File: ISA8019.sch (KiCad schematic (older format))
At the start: 22 parts

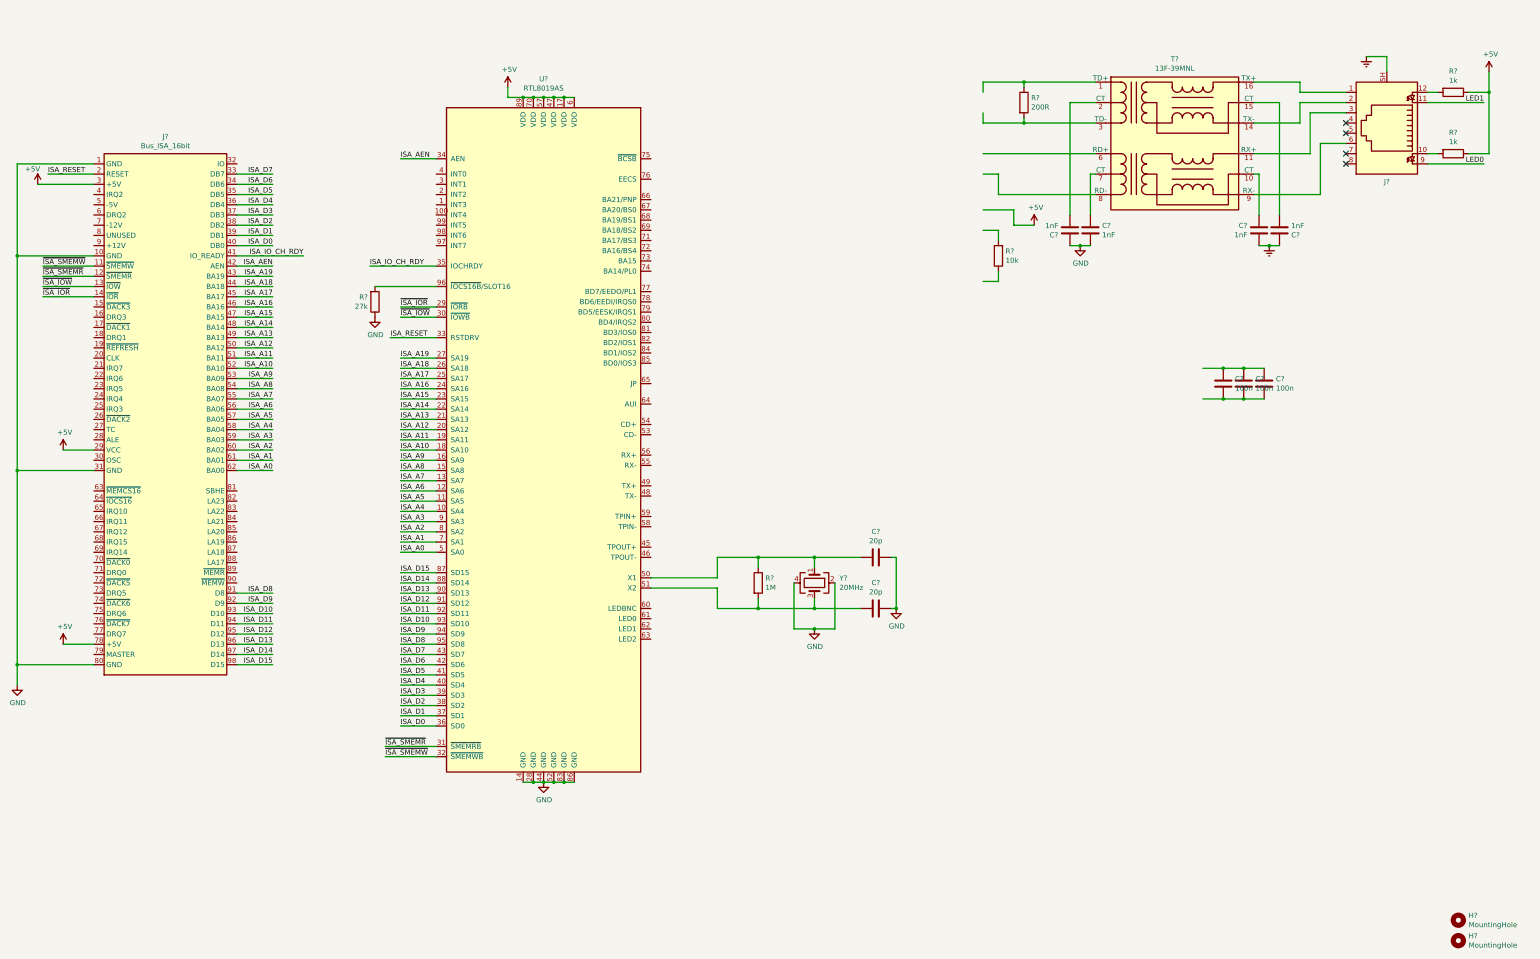
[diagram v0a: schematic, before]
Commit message: Add EEPROM and boot flash
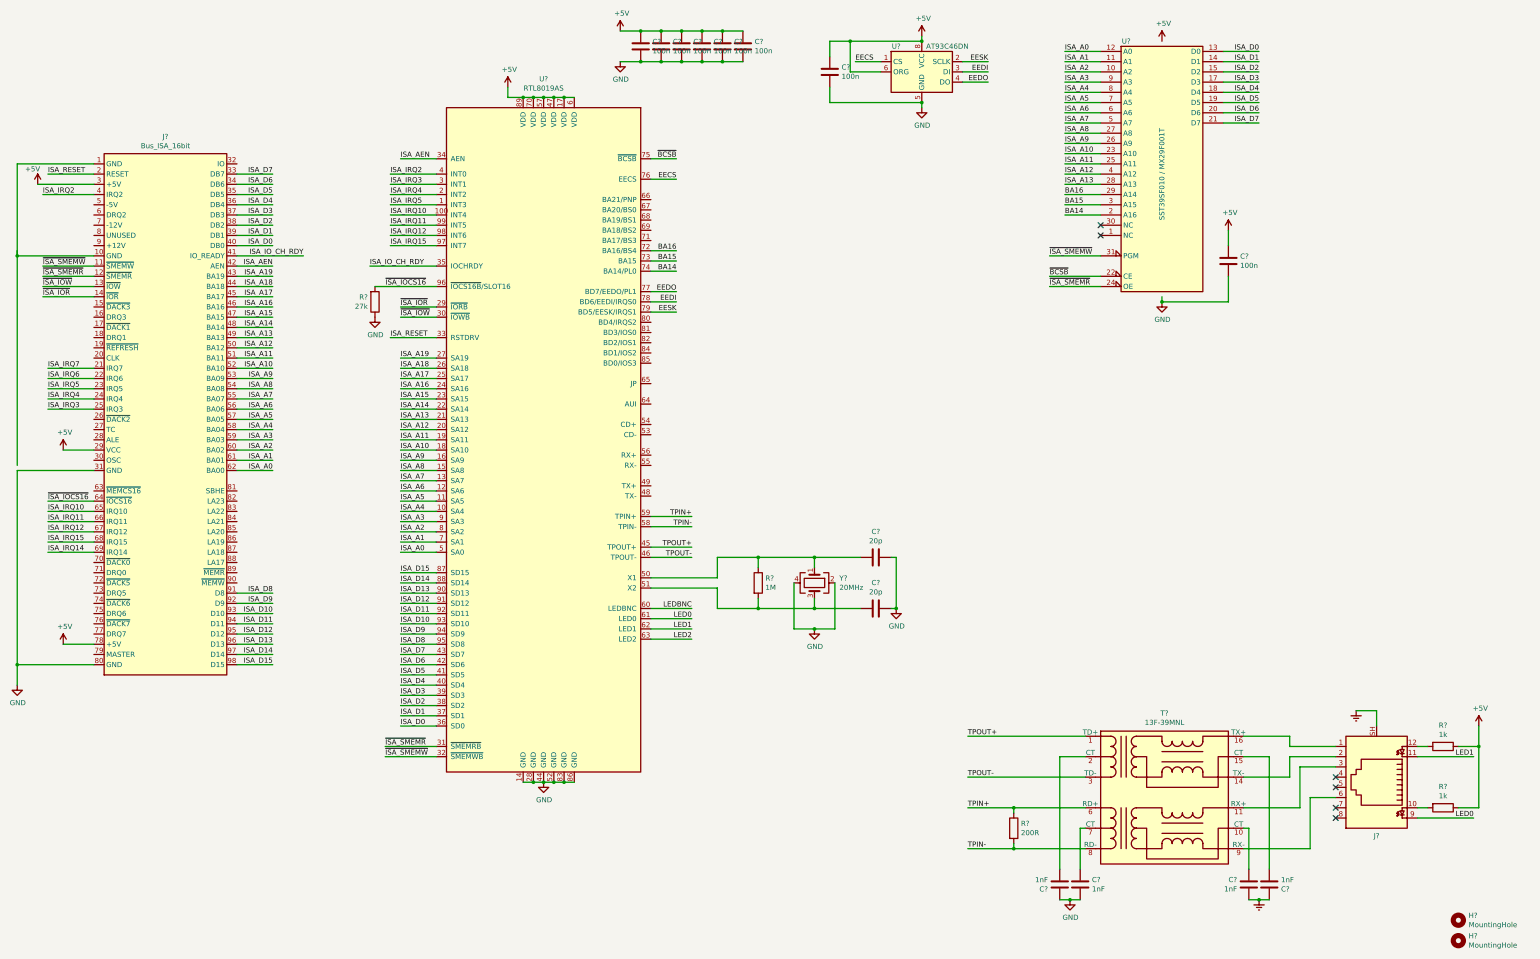
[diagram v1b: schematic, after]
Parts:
- removed R?: 10k, Resistor_SMD:R_0402_1005Metric, symbol Device:R
- added C? (x5): 100n, Capacitor_SMD:C_0402_1005Metric, symbol Device:C
- added U?: AT93C46DN, Package_SO:SOIC-8_3.9x4.9mm_P1.27mm, symbol Memory_EEPROM:93CxxC
- added U?: SST39SF010 / MX29F001T, Package_DIP:DIP-32_W15.24mm_Socket_LongPads, symbol Memory_Flash:SST39SF010
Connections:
- net labels added: BA14, BA15, BA16, EECS, EEDI, EEDO, EESK, ISA_IRQ10, ISA_IRQ11, ISA_IRQ12, ISA_IRQ14, ISA_IRQ15, ISA_IRQ2, ISA_IRQ3, ISA_IRQ4, ISA_IRQ5, ISA_IRQ6, ISA_IRQ7, LED2, LEDBNC, TPIN+, TPIN-, TPOUT+, TPOUT-, ~BCSB, ~ISA_IOCS16
- wire segments 190 -> 267
- no-connect marks 4 -> 6
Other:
- moved on the sheet: C?, J?, R?, T?

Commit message: Add jumpers, AUI interface
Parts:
- removed C? (x5): 100n, Capacitor_SMD:C_0402_1005Metric, symbol Device:C
- added C15, C3, C4, C5, C6: 100n, Capacitor_SMD:C_0402_1005Metric, symbol Device:C
- added C2: 47µF 10V, Capacitor_SMD:C_1206_3216Metric, symbol Device:C
- added J3: AUI, Connector_PinHeader_2.54mm:PinHeader_2x08_P2.54mm_Vertical, symbol Connector_Generic:Conn_02x08_Top_Bottom
- added J4: Jumper mode, Connector_PinHeader_2.54mm:PinHeader_2x01_P2.54mm_Vertical, symbol Connector_Generic:Conn_02x01
- added J5: PNP force, Connector_PinHeader_2.54mm:PinHeader_2x01_P2.54mm_Vertical, symbol Connector_Generic:Conn_02x01
- added J6: BROM size and base address, Connector_PinHeader_2.54mm:PinHeader_2x05_P2.54mm_Vertical, symbol Connector_Generic:Conn_02x05_Counter_Clockwise
- added J7: I/O base address, Connector_PinHeader_2.54mm:PinHeader_2x04_P2.54mm_Vertical, symbol Connector_Generic:Conn_02x04_Counter_Clockwise
- added J8: Medium type, Connector_PinHeader_2.54mm:PinHeader_2x02_P2.54mm_Vertical, symbol Connector_Generic:Conn_02x02_Counter_Clockwise
- added J9: IRQ select, Connector_PinHeader_2.54mm:PinHeader_2x03_P2.54mm_Vertical, symbol Connector_Generic:Conn_02x03_Counter_Clockwise
- added R10, R11, R12, R13, R14, R15, R16, R17, R18, R19, R20, R21, R22, R6, R7, R8, R9: 10k, Resistor_SMD:R_0402_1005Metric, symbol Device:R
- J1: renamed from J?; footprint (none) -> Connector_PCBEdge:BUS_AT
- gave numbers to parts that had none: 22
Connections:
- net +5V: now also C15.1, C2.1, C3.1, C4.1, C5.1, C6.1, J4.2 (Pin_2), J5.2 (Pin_2), J6.10 (Pin_10), J6.6 (Pin_6), J6.7 (Pin_7), J6.8 (Pin_8), J6.9 (Pin_9), J7.5 (Pin_5), J7.6 (Pin_6), J7.7 (Pin_7), J7.8 (Pin_8), J8.3 (Pin_3), J8.4 (Pin_4), J9.4 (Pin_4), J9.5 (Pin_5), J9.6 (Pin_6)
- net BA14: now also R18.1
- net BA16: now also R13.1
- net GND: now also J1.1 (GND), J1.10 (GND), C15.2, C2.2, C3.2, C4.2, C5.2, C6.2, J3.1 (Pin_1), J3.11 (Pin_11), J3.14 (Pin_14), J3.4 (Pin_4), J3.6 (Pin_6), J3.8 (Pin_8), R6.2
- net ISA_D0: no longer U3.13 (D0)
- net ISA_D1: no longer U3.14 (D1)
- net ISA_D2: no longer U3.15 (D2)
- net ISA_D3: no longer U3.17 (D3)
- net ISA_D4: no longer U3.18 (D4)
- net ISA_D5: no longer U3.19 (D5)
- net ISA_D6: no longer U3.20 (D6)
- net ISA_D7: no longer U3.21 (D7)
- net +12V: now reaches J1.9 (+12V)
- net +12V: now also J3.13 (Pin_13)
- net TX-: now reaches U1.48 (TX-)
- net TX-: now also J3.10 (Pin_10)
- net TX+: now reaches U1.49 (TX+)
- net TX+: now also J3.3 (Pin_3)
- net CD-: now reaches U1.53 (CD-)
- net CD-: now also J3.9 (Pin_9)
- net CD+: now reaches U1.54 (CD+)
- net CD+: now also J3.2 (Pin_2)
- net RX-: now reaches U1.55 (RX-)
- net RX-: now also J3.12 (Pin_12)
- net RX+: now reaches U1.56 (RX+)
- net RX+: now also J3.5 (Pin_5)
- net AUI: now reaches U1.64 (AUI)
- net AUI: now also J3.16 (Pin_16), R6.1
- net JP: now reaches U1.65 (JP)
- net JP: now also R7.1
- net PNP: now reaches U1.66 (BA21/PNP)
- net PNP: now also R8.1
- net BS0: now reaches U1.67 (BA20/BS0)
- net BS0: now also R9.1
- net BS1: now reaches U1.68 (BA19/BS1)
- net BS1: now also R10.1
- net BS2: now reaches U1.69 (BA18/BS2)
- net BS2: now also R11.1
- net BS3: now reaches U1.71 (BA17/BS3)
- net BS3: now also R12.1
- net BD4: now reaches U1.80 (BD4/IRQS2)
- net BD4: now also U3.18 (D4), R22.1
- net BD3: now reaches U1.81 (BD3/IOS0)
- net BD3: now also U3.17 (D3), R14.1
- net BD2: now reaches U1.82 (BD2/IOS1)
- net BD2: now also U3.15 (D2), R15.1
- net BD1: now reaches U1.84 (BD1/IOS2)
- net BD1: now also U3.14 (D1), R16.1
- net BD0: now reaches U1.85 (BD0/IOS3)
- net BD0: now also U3.13 (D0), R17.1
- net EEDI renamed BD6
- net BD6: now also U3.20 (D6), R20.1
- net EEDO renamed BD7
- net BD7: now also U3.21 (D7), R19.1
- net EESK renamed BD5
- net BD5: now also U3.19 (D5), R21.1
- new net: J6.1 (Pin_1), R9.2
- new net: J6.2 (Pin_2), R10.2
- new net: J6.3 (Pin_3), R11.2
- new net: J6.4 (Pin_4), R12.2
- new net: J6.5 (Pin_5), R13.2
- new net: J4.1 (Pin_1), R7.2
- new net: J7.1 (Pin_1), R14.2
- new net: J7.2 (Pin_2), R15.2
- new net: J7.3 (Pin_3), R16.2
- new net: J7.4 (Pin_4), R17.2
- new net: J8.1 (Pin_1), R18.2
- new net: J8.2 (Pin_2), R19.2
- new net: J9.1 (Pin_1), R20.2
- new net: J9.2 (Pin_2), R21.2
- new net: J9.3 (Pin_3), R22.2
- new net: J5.1 (Pin_1), R8.2
- no-connect marks 6 -> 8
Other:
- note added: "Base-T Interface"
- note added: "Boot ROM"
- note added: "EEPROM"
- note added: "ISA-Bus"
- note added: "Jumpers"
- note added: "RTL8019"
- moved on the sheet: C1, C12, C7, J1, U2, U3

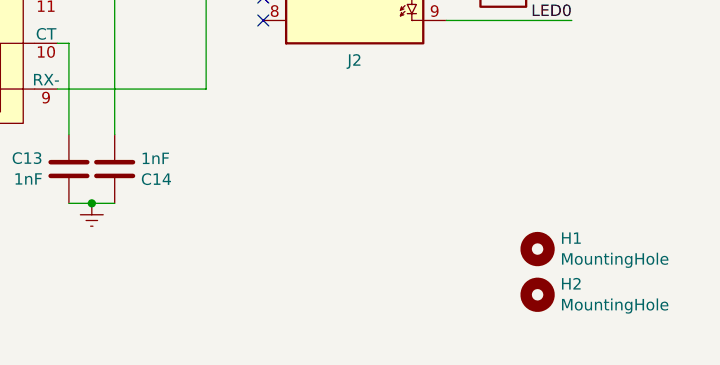
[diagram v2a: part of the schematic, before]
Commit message: Add mechanicals
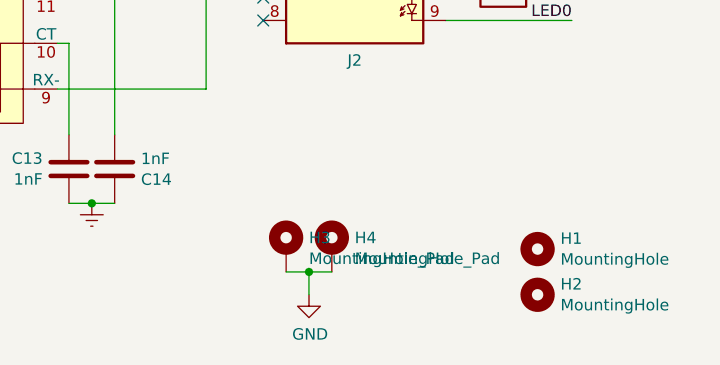
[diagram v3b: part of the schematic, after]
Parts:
- added H3, H4: MountingHole_Pad, MountingHole:MountingHole_3.2mm_M3_Pad_Via, symbol Mechanical:MountingHole_Pad
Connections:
- net GND: now also H3.1, H4.1
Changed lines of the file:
@@
 Wire Wire Line
 	1000 6350 1000 6400
+$Comp
+L Mechanical:MountingHole_Pad H4
+U 1 1 5FB5664A
+P 14350 9450
+F 0 "H4" H 14450 9499 50  0000 L CNN
+F 1 "MountingHole_Pad" H 14450 9408 50  0000 L CNN
+F 2 "MountingHole:MountingHole_3.2mm_M3_Pad_Via" H 14350 9450 50  0001 C CNN
+F 3 "~" H 14350 9450 50  0001 C CNN
+	1    14350 9450
+	1    0    0    -1
+$EndComp
+$Comp
+L Mechanical:MountingHole_Pad H3
+U 1 1 5FB57285
+P 14150 9450
+F 0 "H3" H 14250 9499 50  0000 L CNN
+F 1 "MountingHole_Pad" H 14250 9408 50  0000 L CNN
+F 2 "MountingHole:MountingHole_3.2mm_M3_Pad_Via" H 14150 9450 50  0001 C CNN
+F 3 "~" H 14150 9450 50  0001 C CNN
+	1    14150 9450
+	1    0    0    -1
+$EndComp
+$Comp
+L power:GND #PWR0128
+U 1 1 5FB8A9FE
+P 14250 9650
+F 0 "#PWR0128" H 14250 9400 50  0001 C CNN
+F 1 "GND" H 14255 9477 50  0000 C CNN
+F 2 "" H 14250 9650 50  0001 C CNN
+F 3 "" H 14250 9650 50  0001 C CNN
+	1    14250 9650
+	1    0    0    -1
+$EndComp
+Wire Wire Line
+	14150 9550 14250 9550
+Wire Wire Line
+	14250 9550 14250 9650
+Connection ~ 14250 9550
+Wire Wire Line
+	14250 9550 14350 9550
 $EndSCHEMATC

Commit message: Some routing
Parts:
- removed J3: AUI, Connector_PinHeader_2.54mm:PinHeader_2x08_P2.54mm_Vertical, symbol Connector_Generic:Conn_02x08_Top_Bottom
- added FB1: Ferrite_Bead, Inductor_SMD:L_0805_2012Metric, symbol Device:Ferrite_Bead
- J6: symbol Connector_Generic:Conn_02x05_Counter_Clockwise -> Connector_Generic:Conn_02x05_Odd_Even
- J7: symbol Connector_Generic:Conn_02x04_Counter_Clockwise -> Connector_Generic:Conn_02x04_Odd_Even
- J8: symbol Connector_Generic:Conn_02x02_Counter_Clockwise -> Connector_Generic:Conn_02x02_Odd_Even
- J9: symbol Connector_Generic:Conn_02x03_Counter_Clockwise -> Connector_Generic:Conn_02x03_Odd_Even
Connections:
- net +5V: now also J6.2 (Pin_2), J6.4 (Pin_4), J7.2 (Pin_2), J7.4 (Pin_4), J8.2 (Pin_2), J9.2 (Pin_2); no longer J6.7 (Pin_7), J6.9 (Pin_9), J7.5 (Pin_5), J7.7 (Pin_7), J8.3 (Pin_3), J9.5 (Pin_5)
- net Earth: now also FB1.1
- net GND: now also FB1.2
- net at C8.2, R2.1, U1.50 (X1): now also Y1.3; no longer Y1.1
- net at C9.2, R2.2, U1.51 (X2): now also Y1.1; no longer Y1.3
- net at J6.1 (Pin_1): now also R13.2; no longer R9.2
- net at R10.2: now also J6.7 (Pin_7); no longer J6.2 (Pin_2)
- net at J6.3 (Pin_3): now also R12.2; no longer R11.2
- net at J6.5 (Pin_5): now also R11.2; no longer R13.2
- net at R15.2: now also J7.3 (Pin_3); no longer J7.2 (Pin_2)
- net at R16.2: now also J7.5 (Pin_5); no longer J7.3 (Pin_3)
- net at R17.2: now also J7.7 (Pin_7); no longer J7.4 (Pin_4)
- net at R19.2: now also J8.3 (Pin_3); no longer J8.2 (Pin_2)
- net at R21.2: now also J9.3 (Pin_3); no longer J9.2 (Pin_2)
- net at R22.2: now also J9.5 (Pin_5); no longer J9.3 (Pin_3)
- new net: J6.9 (Pin_9), R9.2
- no-connect marks 8 -> 6
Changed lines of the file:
@@
 F 4 "C110936" V 8950 6150 50  0001 C CNN "LCSC"
 	1    8950 6150
-	0    1    1    0
+	0    1    -1   0
 $EndComp
 Wire Wire Line
@@
 	7350 2000 7600 2000
 $Comp
-L Connector_Generic:Conn_02x05_Counter_Clockwise J6
+L Connector_Generic:Conn_02x05_Odd_Even J6
 U 1 1 605952D4
 P 14850 2650
 F 0 "J6" H 14900 3067 50  0000 C CNN
-F 1 "BROM size and base address" H 14900 2976 50  0000 C CNN
+F 1 "BROM size and base address" H 14900 2300 50  0000 C CNN
 F 2 "Connector_PinHeader_2.54mm:PinHeader_2x05_P2.54mm_Vertical" H 14850 2650 50  0001 C CNN
 F 3 "~" H 14850 2650 50  0001 C CNN
 	1    14850 2650
-	1    0    0    -1
+	1    0    0    1
 $EndComp
 $Comp
@@
 $EndComp
 $Comp
-L Connector_Generic:Conn_02x04_Counter_Clockwise J7
+L Connector_Generic:Conn_02x04_Odd_Even J7
 U 1 1 605EB97F
 P 14850 3300
@@
 $EndComp
 $Comp
-L Connector_Generic:Conn_02x02_Counter_Clockwise J8
+L Connector_Generic:Conn_02x02_Odd_Even J8
 U 1 1 605ED14C
 P 14850 3850
@@
 $EndComp
 $Comp
-L Connector_Generic:Conn_02x03_Counter_Clockwise J9
+L Connector_Generic:Conn_02x03_Odd_Even J9
 U 1 1 605EED03
 P 14850 4400
@@
 Wire Wire Line
 	5550 8950 5800 8950
-$Comp
-L Connector_Generic:Conn_02x08_Top_Bottom J3
-U 1 1 61CBB166
-P 9150 4750
-F 0 "J3" H 9200 5267 50  0000 C CNN
-F 1 "AUI" H 9200 5176 50  0000 C CNN
-F 2 "Connector_PinHeader_2.54mm:PinHeader_2x08_P2.54mm_Vertical" H 9150 4750 50  0001 C CNN
-F 3 "~" H 9150 4750 50  0001 C CNN
-	1    9150 4750
-	1    0    0    -1
-$EndComp
-NoConn ~ 8950 5050
-NoConn ~ 9450 5050
-$Comp
-L power:GND #PWR0123
-U 1 1 61DC086B
-P 8850 5250
-F 0 "#PWR0123" H 8850 5000 50  0001 C CNN
-F 1 "GND" H 8855 5077 50  0000 C CNN
-F 2 "" H 8850 5250 50  0001 C CNN
-F 3 "" H 8850 5250 50  0001 C CNN
-	1    8850 5250
-	1    0    0    -1
-$EndComp
-Wire Wire Line
-	8950 4450 8850 4450
-Wire Wire Line
-	8850 4450 8850 4750
-Wire Wire Line
-	8950 4750 8850 4750
-Connection ~ 8850 4750
-Wire Wire Line
-	8850 4750 8850 4950
-Wire Wire Line
-	8950 4950 8850 4950
-Connection ~ 8850 4950
-Wire Wire Line
-	8850 4950 8850 5150
-Wire Wire Line
-	8950 5150 8850 5150
-Connection ~ 8850 5150
-Wire Wire Line
-	8850 5150 8850 5250
-Wire Wire Line
-	9450 4650 9550 4650
-Wire Wire Line
-	9550 4650 9550 4950
-Wire Wire Line
-	9550 4950 9450 4950
-Wire Wire Line
-	9550 4950 9550 5250
-Connection ~ 9550 4950
-$Comp
-L power:GND #PWR0124
-U 1 1 61EFBDD1
-P 9550 5250
-F 0 "#PWR0124" H 9550 5000 50  0001 C CNN
-F 1 "GND" H 9555 5077 50  0000 C CNN
-F 2 "" H 9550 5250 50  0001 C CNN
-F 3 "" H 9550 5250 50  0001 C CNN
-	1    9550 5250
-	1    0    0    -1
-$EndComp
-Text Label 8650 4550 0    50   ~ 0
-CD+
-Wire Wire Line
-	8650 4550 8950 4550
-Text Label 8650 4650 0    50   ~ 0
-TX+
-Text Label 8650 4850 0    50   ~ 0
-RX+
-Text Label 9700 4450 2    50   ~ 0
-CD-
-Text Label 9700 4550 2    50   ~ 0
-TX-
-Text Label 9700 4750 2    50   ~ 0
-RX-
-$Comp
-L power:+12V #PWR0125
-U 1 1 61F3055B
-P 9900 4350
-F 0 "#PWR0125" H 9900 4200 50  0001 C CNN
-F 1 "+12V" H 9915 4523 50  0000 C CNN
-F 2 "" H 9900 4350 50  0001 C CNN
-F 3 "" H 9900 4350 50  0001 C CNN
-	1    9900 4350
-	1    0    0    -1
-$EndComp
-Wire Wire Line
-	9450 4850 9900 4850
-Wire Wire Line
-	9900 4350 9900 4850
-Wire Wire Line
-	9700 4750 9450 4750
-Wire Wire Line
-	9450 4450 9700 4450
-Wire Wire Line
-	8650 4650 8950 4650
-Wire Wire Line
-	8650 4850 8950 4850
 Text Label 7600 4600 2    50   ~ 0
 CD+
@@
 Wire Wire Line
 	1750 2300 2300 2300
-Wire Wire Line
-	9450 4550 9700 4550
 Text Label 7600 4400 2    50   ~ 0
 AUI
 Wire Wire Line
 	7350 4400 7700 4400
-Text Label 9700 5150 2    50   ~ 0
-AUI
-Wire Wire Line
-	9700 5150 9450 5150
 Wire Wire Line
 	1000 6350 1000 6400
@@
 Wire Wire Line
 	14250 9550 14350 9550
+$Comp
+L power:Earth #PWR0129
+U 1 1 5FC46E93
+P 12700 9500
+F 0 "#PWR0129" H 12700 9250 50  0001 C CNN
+F 1 "Earth" H 12700 9350 50  0001 C CNN
+F 2 "" H 12700 9500 50  0001 C CNN
+F 3 "~" H 12700 9500 50  0001 C CNN
+	1    12700 9500
+	1    0    0    -1
+$EndComp
+$Comp
+L Device:Ferrite_Bead FB1
+U 1 1 5FC47DE8
+P 12550 9450
+F 0 "FB1" V 12276 9450 50  0000 C CNN
+F 1 "Ferrite_Bead" V 12367 9450 50  0000 C CNN
+F 2 "Inductor_SMD:L_0805_2012Metric" V 12480 9450 50  0001 C CNN
+F 3 "~" H 12550 9450 50  0001 C CNN
+F 4 "C1017" V 12550 9450 50  0001 C CNN "LCSC"
+	1    12550 9450
+	0    1    1    0
+$EndComp
+$Comp
+L power:GND #PWR0130
+U 1 1 5FC496B0
+P 12400 9500
+F 0 "#PWR0130" H 12400 9250 50  0001 C CNN
+F 1 "GND" H 12405 9327 50  0000 C CNN
+F 2 "" H 12400 9500 50  0001 C CNN
+F 3 "" H 12400 9500 50  0001 C CNN
+	1    12400 9500
+	1    0    0    -1
+$EndComp
+Wire Wire Line
+	12400 9450 12400 9500
+Wire Wire Line
+	12700 9450 12700 9500
 $EndSCHEMATC
